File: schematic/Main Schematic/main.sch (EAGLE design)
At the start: 52 parts, among them IC1 STM32F103C8T6, IC3 DRV8836, IC4 MCP73831, IC5 MCP1825S-3302E/DB, Y1 8MHz

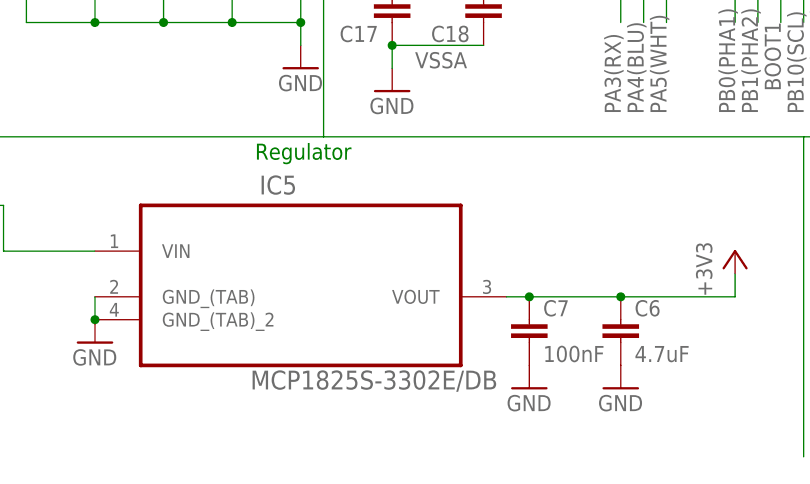
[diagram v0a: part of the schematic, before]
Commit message: Replaced 1825 with 1826 regulator in Schematic, added PNG
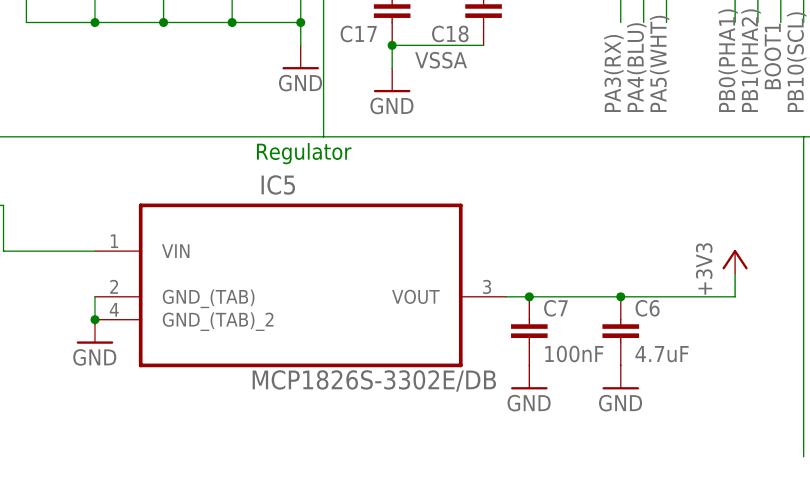
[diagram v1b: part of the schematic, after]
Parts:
- IC5: value MCP1825S-3302E/DB -> MCP1826S-3302E/DB; device MCP1825S-3302E_DB:MCP1825S-3302E/DB -> MCP1826S-3302E_DB:MCP1826S-3302E/DB
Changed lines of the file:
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@@
 <grid distance="0.1" unitdist="inch" unit="inch" style="lines" multiple="1" display="no" altdistance="0.01" altunitdist="inch" altunit="inch"/>
 <layers>
-<layer number="1" name="Top" color="4" fill="1" visible="yes" active="no"/>
-<layer number="2" name="Route2" color="1" fill="3" visible="yes" active="no"/>
-<layer number="3" name="Route3" color="4" fill="3" visible="yes" active="no"/>
-<layer number="4" name="Route4" color="1" fill="4" visible="yes" active="no"/>
-<layer number="5" name="Route5" color="4" fill="4" visible="yes" active="no"/>
-<layer number="6" name="Route6" color="1" fill="8" visible="yes" active="no"/>
-<layer number="7" name="Route7" color="4" fill="8" visible="yes" active="no"/>
-<layer number="8" name="Route8" color="1" fill="2" visible="yes" active="no"/>
-<layer number="9" name="Route9" color="4" fill="2" visible="yes" active="no"/>
-<layer number="10" name="Route10" color="1" fill="7" visible="yes" active="no"/>
-<layer number="11" name="Route11" color="4" fill="7" visible="yes" active="no"/>
-<layer number="12" name="Route12" color="1" fill="5" visible="yes" active="no"/>
-<layer number="13" name="Route13" color="4" fill="5" visible="yes" active="no"/>
-<layer number="14" name="Route14" color="1" fill="6" visible="yes" active="no"/>
-<layer number="15" name="Route15" color="4" fill="6" visible="yes" active="no"/>
-<layer number="16" name="Bottom" color="1" fill="1" visible="yes" active="no"/>
-<layer number="17" name="Pads" color="2" fill="1" visible="yes" active="no"/>
-<layer number="18" name="Vias" color="2" fill="1" visible="yes" active="no"/>
-<layer number="19" name="Unrouted" color="6" fill="1" visible="yes" active="no"/>
-<layer number="20" name="Dimension" color="15" fill="1" visible="yes" active="no"/>
-<layer number="21" name="tPlace" color="7" fill="1" visible="yes" active="no"/>
-<layer number="22" name="bPlace" color="7" fill="1" visible="yes" active="no"/>
-<layer number="23" name="tOrigins" color="15" fill="1" visible="yes" active="no"/>
-<layer number="24" name="bOrigins" color="15" fill="1" visible="yes" active="no"/>
-<layer number="25" name="tNames" color="7" fill="1" visible="yes" active="no"/>
-<layer number="26" name="bNames" color="7" fill="1" visible="yes" active="no"/>
-<layer number="27" name="tValues" color="7" fill="1" visible="yes" active="no"/>
-<layer number="28" name="bValues" color="7" fill="1" visible="yes" active="no"/>
+<layer number="1" name="Top" color="4" fill="1" visible="no" active="no"/>
+<layer number="2" name="Route2" color="1" fill="3" visible="no" active="no"/>
+<layer number="3" name="Route3" color="4" fill="3" visible="no" active="no"/>
+<layer number="4" name="Route4" color="1" fill="4" visible="no" active="no"/>
+<layer number="5" name="Route5" color="4" fill="4" visible="no" active="no"/>
+<layer number="6" name="Route6" color="1" fill="8" visible="no" active="no"/>
+<layer number="7" name="Route7" color="4" fill="8" visible="no" active="no"/>
+<layer number="8" name="Route8" color="1" fill="2" visible="no" active="no"/>
+<layer number="9" name="Route9" color="4" fill="2" visible="no" active="no"/>
+<layer number="10" name="Route10" color="1" fill="7" visible="no" active="no"/>
+<layer number="11" name="Route11" color="4" fill="7" visible="no" active="no"/>
+<layer number="12" name="Route12" color="1" fill="5" visible="no" active="no"/>
+<layer number="13" name="Route13" color="4" fill="5" visible="no" active="no"/>
+<layer number="14" name="Route14" color="1" fill="6" visible="no" active="no"/>
+<layer number="15" name="Route15" color="4" fill="6" visible="no" active="no"/>
+<layer number="16" name="Bottom" color="1" fill="1" visible="no" active="no"/>
+<layer number="17" name="Pads" color="2" fill="1" visible="no" active="no"/>
+<layer number="18" name="Vias" color="2" fill="1" visible="no" active="no"/>
+<layer number="19" name="Unrouted" color="6" fill="1" visible="no" active="no"/>
+<layer number="20" name="Dimension" color="15" fill="1" visible="no" active="no"/>
+<layer number="21" name="tPlace" color="7" fill="1" visible="no" active="no"/>
+<layer number="22" name="bPlace" color="7" fill="1" visible="no" active="no"/>
+<layer number="23" name="tOrigins" color="15" fill="1" visible="no" active="no"/>
+<layer number="24" name="bOrigins" color="15" fill="1" visible="no" active="no"/>
+<layer number="25" name="tNames" color="7" fill="1" visible="no" active="no"/>
+<layer number="26" name="bNames" color="7" fill="1" visible="no" active="no"/>
+<layer number="27" name="tValues" color="7" fill="1" visible="no" active="no"/>
+<layer number="28" name="bValues" color="7" fill="1" visible="no" active="no"/>
 <layer number="29" name="tStop" color="7" fill="3" visible="no" active="no"/>
 <layer number="30" name="bStop" color="7" fill="6" visible="no" active="no"/>
@@
 <layer number="35" name="tGlue" color="7" fill="4" visible="no" active="no"/>
 <layer number="36" name="bGlue" color="7" fill="5" visible="no" active="no"/>
-<layer number="37" name="tTest" color="7" fill="1" visible="yes" active="no"/>
-<layer number="38" name="bTest" color="7" fill="1" visible="yes" active="no"/>
+<layer number="37" name="tTest" color="7" fill="1" visible="no" active="no"/>
+<layer number="38" name="bTest" color="7" fill="1" visible="no" active="no"/>
 <layer number="39" name="tKeepout" color="4" fill="11" visible="no" active="no"/>
 <layer number="40" name="bKeepout" color="1" fill="11" visible="no" active="no"/>
@@
 <layer number="44" name="Drills" color="7" fill="1" visible="no" active="no"/>
 <layer number="45" name="Holes" color="7" fill="1" visible="no" active="no"/>
-<layer number="46" name="Milling" color="3" fill="1" visible="yes" active="no"/>
-<layer number="47" name="Measures" color="7" fill="1" visible="yes" active="no"/>
-<layer number="48" name="Document" color="7" fill="1" visible="yes" active="no"/>
-<layer number="49" name="Reference" color="7" fill="1" visible="yes" active="no"/>
-<layer number="50" name="dxf" color="7" fill="1" visible="yes" active="no"/>
-<layer number="51" name="tDocu" color="7" fill="1" visible="yes" active="no"/>
-<layer number="52" name="bDocu" color="7" fill="1" visible="yes" active="no"/>
-<layer number="53" name="tGND_GNDA" color="7" fill="9" visible="yes" active="no"/>
-<layer number="54" name="bGND_GNDA" color="1" fill="9" visible="yes" active="no"/>
-<layer number="56" name="wert" color="7" fill="1" visible="yes" active="no"/>
-<layer number="57" name="tCAD" color="7" fill="1" visible="yes" active="no"/>
-<layer number="59" name="tCarbon" color="7" fill="1" visible="yes" active="no"/>
-<layer number="60" name="bCarbon" color="7" fill="1" visible="yes" active="no"/>
+<layer number="46" name="Milling" color="3" fill="1" visible="no" active="no"/>
+<layer number="47" name="Measures" color="7" fill="1" visible="no" active="no"/>
+<layer number="48" name="Document" color="7" fill="1" visible="no" active="no"/>
+<layer number="49" name="Reference" color="7" fill="1" visible="no" active="no"/>
+<layer number="50" name="dxf" color="7" fill="1" visible="no" active="no"/>
+<layer number="51" name="tDocu" color="7" fill="1" visible="no" active="no"/>
+<layer number="52" name="bDocu" color="7" fill="1" visible="no" active="no"/>
+<layer number="53" name="tGND_GNDA" color="7" fill="9" visible="no" active="no"/>
+<layer number="54" name="bGND_GNDA" color="1" fill="9" visible="no" active="no"/>
+<layer number="56" name="wert" color="7" fill="1" visible="no" active="no"/>
+<layer number="57" name="tCAD" color="7" fill="1" visible="no" active="no"/>
+<layer number="59" name="tCarbon" color="7" fill="1" visible="no" active="no"/>
+<layer number="60" name="bCarbon" color="7" fill="1" visible="no" active="no"/>
 <layer number="90" name="Modules" color="5" fill="1" visible="yes" active="yes"/>
 <layer number="91" name="Nets" color="2" fill="1" visible="yes" active="yes"/>
@@
 <part name="USB" library="daspilker" deviceset="USB-RECEPTABLE" device=""/>
 <part name="GND9" library="supply1" library_urn="urn:adsk.eagle:library:371" deviceset="GND" device=""/>
-<part name="IC5" library="MCP1825S-3302E_DB" deviceset="MCP1825S-3302E/DB" device=""/>
+<part name="IC5" library="MCP1826S-3302E_DB" deviceset="MCP1826S-3302E/DB" device=""/>
 <part name="CHG" library="eagle-ltspice" library_urn="urn:adsk.eagle:library:217" deviceset="LED_E" device="SML0603" package3d_urn="urn:adsk.eagle:package:13315/1"/>
 <part name="PWR" library="eagle-ltspice" library_urn="urn:adsk.eagle:library:217" deviceset="LED_E" device="SML0603" package3d_urn="urn:adsk.eagle:package:13315/1"/>

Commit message: Misc Errata, Schematic v 0.8
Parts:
- added R15: 330, resistor:R-EU_R0603
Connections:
- new net N$1: C12.2, R15.2
- net +3V3: no longer IC1.VDD1
- net GND: no longer IC1.VSS1
- net N$15: now also R15.1; no longer C12.2
- net VDD1: now also IC1.VDD1
- net VSS1: now also IC1.VSS1
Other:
- moved on the sheet: C12
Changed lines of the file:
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@@
 <part name="FRAME1" library="SparkFun-Aesthetics" library_urn="urn:adsk.eagle:library:507" deviceset="FRAME-A4L" device="">
 <attribute name="CNAME" value="HiveX Schematic"/>
-<attribute name="CREVISION" value="0.7"/>
+<attribute name="CREVISION" value="0.8"/>
 <attribute name="DESIGNER" value="Aditya Bhat, Akshay Hegde"/>
 </part>
@@
 <part name="C17" library="SparkFun-Capacitors" deviceset="CAP" device="0603-CAP" value="10nF"/>
 <part name="C18" library="SparkFun-Capacitors" deviceset="CAP" device="0603-CAP" value="500nF"/>
+<part name="R15" library="resistor" library_urn="urn:adsk.eagle:library:348" deviceset="R-EU_" device="R0603" package3d_urn="urn:adsk.eagle:package:26057/1" value="330"/>
 </parts>
 <sheets>
@@
 <instance part="GND15" gate="1" x="-104.14" y="12.7"/>
 <instance part="S1" gate="G$1" x="-55.88" y="111.76" rot="R90"/>
-<instance part="C12" gate="G$1" x="-45.72" y="111.76"/>
+<instance part="C12" gate="G$1" x="-45.72" y="114.3"/>
 <instance part="R8" gate="G$1" x="-45.72" y="129.54" rot="R90"/>
 <instance part="+3V5" gate="G$1" x="-45.72" y="137.16"/>
-<instance part="GND16" gate="1" x="-45.72" y="99.06"/>
+<instance part="GND16" gate="1" x="-45.72" y="96.52"/>
 <instance part="J2" gate="G$1" x="154.94" y="5.08" rot="R270"/>
 <instance part="J1" gate="G$1" x="144.78" y="12.7" rot="R270"/>
@@
 <instance part="+3V4" gate="G$1" x="-25.4" y="30.48"/>
 <instance part="GND19" gate="1" x="-25.4" y="2.54"/>
-<instance part="+3V6" gate="G$1" x="45.72" y="12.7"/>
+<instance part="+3V6" gate="G$1" x="50.8" y="12.7"/>
 <instance part="GND20" gate="1" x="35.56" y="2.54"/>
 <instance part="GND21" gate="1" x="68.58" y="50.8" rot="R90"/>
@@
 <instance part="C17" gate="G$1" x="-15.24" y="10.16" rot="R180"/>
 <instance part="C18" gate="G$1" x="-5.08" y="10.16" rot="R180"/>
+<instance part="R15" gate="G$1" x="-45.72" y="106.68" rot="R90"/>
 </instances>
 <busses>
@@
 </segment>
 <segment>
-<pinref part="IC1" gate="G$1" pin="VSS1"/>
-<pinref part="GND20" gate="1" pin="GND"/>
-<wire x1="35.56" y1="5.08" x2="35.56" y2="10.16" width="0.1524" layer="91"/>
-</segment>
-<segment>
 <pinref part="IC1" gate="G$1" pin="VSS2"/>
 <pinref part="GND21" gate="1" pin="GND"/>
@@
 </segment>
 <segment>
-<pinref part="IC1" gate="G$1" pin="VDD1"/>
-<wire x1="38.1" y1="10.16" x2="45.72" y2="10.16" width="0.1524" layer="91"/>
-<pinref part="+3V6" gate="G$1" pin="+3V3"/>
-</segment>
-<segment>
 <pinref part="+3V8" gate="G$1" pin="+3V3"/>
 <pinref part="IC1" gate="G$1" pin="VDD3"/>
@@
 <net name="RESET" class="0">
 <segment>
+<pinref part="C12" gate="G$1" pin="1"/>
+<pinref part="R8" gate="G$1" pin="1"/>
+<wire x1="-45.72" y1="124.46" x2="-45.72" y2="121.92" width="0.1524" layer="91"/>
+<wire x1="-45.72" y1="121.92" x2="-45.72" y2="119.38" width="0.1524" layer="91"/>
 <pinref part="S1" gate="G$1" pin="2"/>
-<pinref part="C12" gate="G$1" pin="1"/>
-<wire x1="-55.88" y1="116.84" x2="-45.72" y2="116.84" width="0.1524" layer="91"/>
-<pinref part="R8" gate="G$1" pin="1"/>
-<wire x1="-45.72" y1="124.46" x2="-45.72" y2="116.84" width="0.1524" layer="91"/>
-<junction x="-45.72" y="116.84"/>
-<wire x1="-45.72" y1="116.84" x2="-35.56" y2="116.84" width="0.1524" layer="91"/>
-<label x="-38.1" y="116.84" size="1.778" layer="95"/>
+<wire x1="-55.88" y1="116.84" x2="-55.88" y2="121.92" width="0.1524" layer="91"/>
+<wire x1="-55.88" y1="121.92" x2="-45.72" y2="121.92" width="0.1524" layer="91"/>
+<junction x="-45.72" y="121.92"/>
+<wire x1="-45.72" y1="121.92" x2="-35.56" y2="121.92" width="0.1524" layer="91"/>
+<label x="-43.18" y="121.92" size="1.778" layer="95"/>
 </segment>
 <segment>
@@
 <net name="N$15" class="0">
 <segment>
-<pinref part="C12" gate="G$1" pin="2"/>
-<wire x1="-45.72" y1="109.22" x2="-45.72" y2="101.6" width="0.1524" layer="91"/>
-<wire x1="-45.72" y1="101.6" x2="-55.88" y2="101.6" width="0.1524" layer="91"/>
+<wire x1="-45.72" y1="99.06" x2="-55.88" y2="99.06" width="0.1524" layer="91"/>
 <pinref part="S1" gate="G$1" pin="1"/>
-<wire x1="-55.88" y1="101.6" x2="-55.88" y2="106.68" width="0.1524" layer="91"/>
+<wire x1="-55.88" y1="99.06" x2="-55.88" y2="106.68" width="0.1524" layer="91"/>
 <pinref part="GND16" gate="1" pin="GND"/>
-<junction x="-45.72" y="101.6"/>
+<pinref part="R15" gate="G$1" pin="1"/>
+<wire x1="-45.72" y1="99.06" x2="-45.72" y2="101.6" width="0.1524" layer="91"/>
+<junction x="-45.72" y="99.06"/>
 </segment>
 </net>
@@
 <label x="-99.06" y="121.92" size="1.778" layer="95"/>
 </segment>
+<segment>
+<pinref part="IC1" gate="G$1" pin="VDD1"/>
+<wire x1="38.1" y1="10.16" x2="50.8" y2="10.16" width="0.1524" layer="91"/>
+<pinref part="+3V6" gate="G$1" pin="+3V3"/>
+<label x="38.1" y="7.62" size="1.778" layer="95"/>
+</segment>
 </net>
 <net name="VSS1" class="0">
@@
 <wire x1="-78.74" y1="111.76" x2="-76.2" y2="111.76" width="0.1524" layer="91"/>
 <label x="-78.74" y="111.76" size="1.778" layer="95"/>
+</segment>
+<segment>
+<pinref part="IC1" gate="G$1" pin="VSS1"/>
+<pinref part="GND20" gate="1" pin="GND"/>
+<wire x1="35.56" y1="5.08" x2="35.56" y2="10.16" width="0.1524" layer="91"/>
+<label x="35.56" y="5.08" size="1.778" layer="95" rot="R90"/>
 </segment>
 </net>
@@
 </segment>
 </net>
+<net name="N$1" class="0">
+<segment>
+<pinref part="C12" gate="G$1" pin="2"/>
+<pinref part="R15" gate="G$1" pin="2"/>
+</segment>
+</net>
